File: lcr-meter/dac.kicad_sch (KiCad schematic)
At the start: 0 parts

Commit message: Added CM4, basics of functionality started
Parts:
- added Q2: NPN, symbol Simulation_SPICE:NPN
- added Q3: PNP, symbol Simulation_SPICE:PNP
- added U1: MCP4921, symbol Analog_DAC:MCP4921
- added U3: MCP601-xOT, Package_TO_SOT_SMD:SOT-23-5, symbol Amplifier_Operational:MCP601-xOT
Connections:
- new net: Q2.2 (B), Q3.2 (B), U3.1
- new net: U1.8 (Vout), U3.3 (+)
- new net +5V: Q2.1 (C), U1.1 (Vdd), U1.6 (Vref), U3.5 (V+)
- new net DAC_SCK: U1.3 (SCK)
- new net DAC_SDI: U1.4 (SDI)
- new net DAC_nCS: U1.2 (~{CS})
- new net GND: Q3.1 (C), U1.5 (~{LDAC}), U1.7 (Vss), U3.2 (V-)
- new net Vout: Q2.3 (E), Q3.3 (E), U3.4 (-)

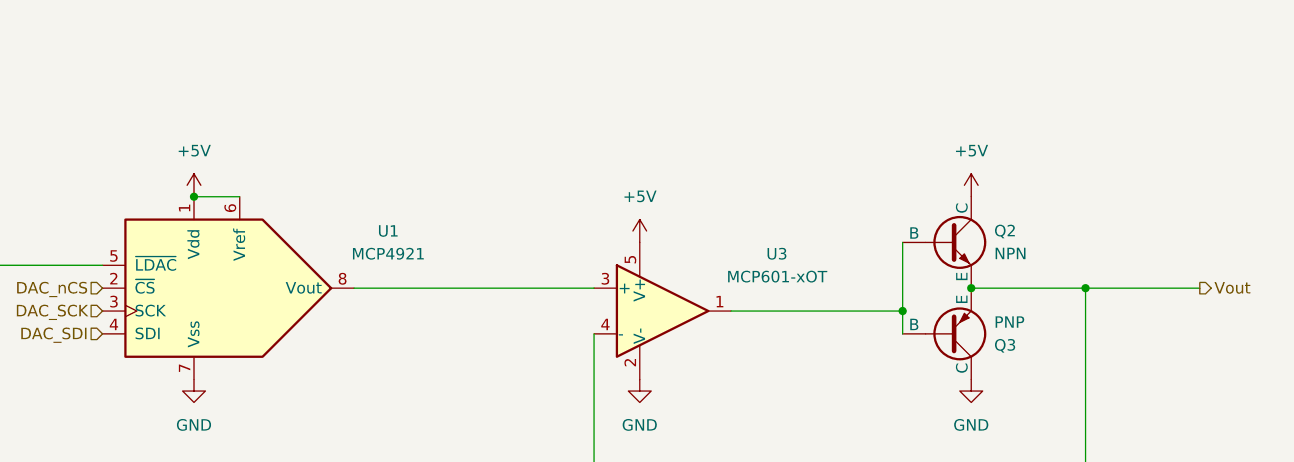
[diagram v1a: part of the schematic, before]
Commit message: Progress, removal of unnecessary components
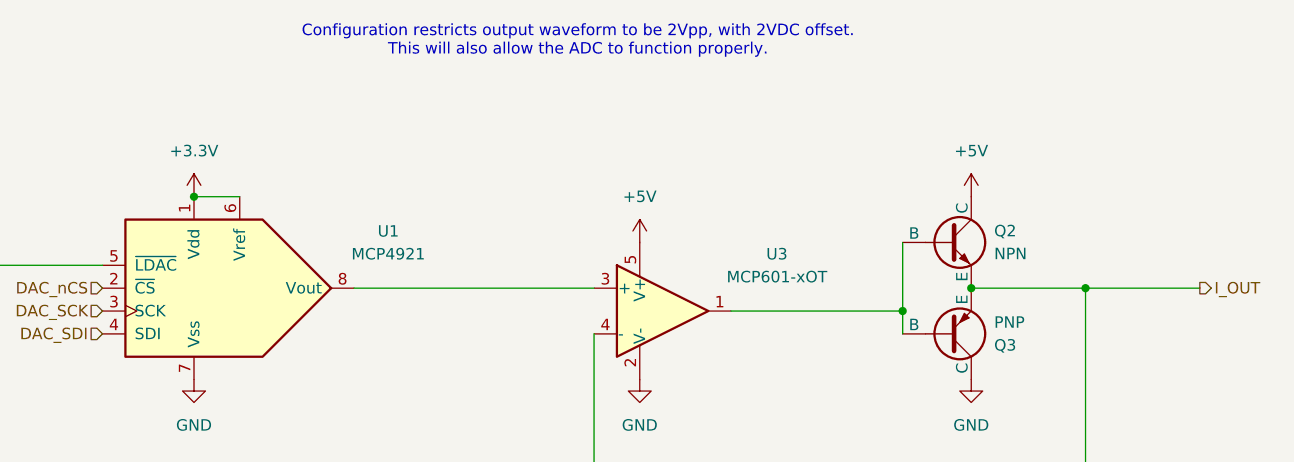
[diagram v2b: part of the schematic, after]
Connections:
- net +5V: no longer U1.1 (Vdd), U1.6 (Vref)
- net Vout renamed I_OUT
- new net +3.3V: U1.1 (Vdd), U1.6 (Vref)
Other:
- note added: "Configuration restricts output waveform to be 2Vpp, with 2VDC offset. This will also allow the ADC to function properly."

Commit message: Breadboarding notes
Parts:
- added U19: AD9833xRM, Package_SO:MSOP-10_3x3mm_P0.5mm, symbol Interface:AD9833xRM
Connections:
- net GND: no longer Q3.1 (C)
- new net -5V: Q3.1 (C)
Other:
- note added: "In testing - BC337"
- note added: "In testing - PN2907A"
- note added: "REPLACE WITH DEDICATED SIGNAL GEN IC AD9833"
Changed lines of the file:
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@@
+		)
+	)
+	(text "In testing - PN2907A"
+		(exclude_from_sim no)
+		(at 232.156 97.79 0)
+		(effects
+			(font
+				(size 1.27 1.27)
+			)
+		)
+	)
+	(text "In testing - BC337"
+		(exclude_from_sim no)
+		(at 232.918 79.248 0)
+		(effects
+			(font
+				(size 1.27 1.27)
+			)
+		)
+	)
+	(text "REPLACE WITH DEDICATED SIGNAL GEN IC\nAD9833"
+		(exclude_from_sim no)
+		(at 101.346 109.982 0)
+		(effects
+			(font
+				(size 1.27 1.27)
+			)
+			(justify left)
 		)
 	)
@@
 	)
 	(symbol
+		(lib_id "power:-5V")
+		(at 213.36 99.06 180)
+		(unit 1)
+		(exclude_from_sim no)
+		(in_bom yes)
+		(on_board yes)
+		(dnp no)
+		(fields_autoplaced yes)
+		(property "Reference" "#PWR059"
+			(at 213.36 95.25 0)
+			(effects
+				(font
+					(size 1.27 1.27)
+				)
+				(hide yes)
+			)
+		)
+		(property "Value" "-5V"
+			(at 213.36 104.14 0)
+			(effects
+				(font
+					(size 1.27 1.27)
+				)
+			)
+		)
+		(property "Footprint" ""
+			(at 213.36 99.06 0)
+			(effects
+				(font
+					(size 1.27 1.27)
+				)
+				(hide yes)
+			)
+		)
+		(property "Datasheet" ""
+			(at 213.36 99.06 0)
+			(effects
+				(font
+					(size 1.27 1.27)
+				)
+				(hide yes)
+			)
+		)
+		(property "Description" "Power symbol creates a global label with name \"-5V\""
+			(at 213.36 99.06 0)
+			(effects
+				(font
+					(size 1.27 1.27)
+				)
+				(hide yes)
+			)
+		)
+		(pin "1"
+		)
+		(instances
+			(project ""
+				(path "/ba333b18-b098-477b-9dd4-aab7b9764d9c/46ee5347-8922-4c9f-a4b3-4d37bef42e8e"
+					(reference "#PWR059")
+					(unit 1)
+				)
+			)
+		)
+	)
+	(symbol
 		(lib_id "power:GND")
 		(at 127 99.06 0)
@@
 	)
 	(symbol
-		(lib_id "power:GND")
-		(at 213.36 99.06 0)
-		(unit 1)
-		(exclude_from_sim no)
-		(in_bom yes)
-		(on_board yes)
-		(dnp no)
-		(fields_autoplaced yes)
-		(property "Reference" "#PWR036"
-			(at 213.36 105.41 0)
-			(effects
-				(font
-					(size 1.27 1.27)
-				)
-				(hide yes)
-			)
-		)
-		(property "Value" "GND"
-			(at 213.36 104.14 0)
-			(effects
-				(font
-					(size 1.27 1.27)
-				)
-			)
-		)
-		(property "Footprint" ""
-			(at 213.36 99.06 0)
-			(effects
-				(font
-					(size 1.27 1.27)
-				)
-				(hide yes)
-			)
-		)
-		(property "Datasheet" ""
-			(at 213.36 99.06 0)
-			(effects
-				(font
-					(size 1.27 1.27)
-				)
-				(hide yes)
-			)
-		)
-		(property "Description" "Power symbol creates a global label with name \"GND\" , ground"
-			(at 213.36 99.06 0)
-			(effects
-				(font
-					(size 1.27 1.27)
-				)
-				(hide yes)
-			)
-		)
-		(pin "1"
-		)
-		(instances
-			(project "lcr-meter"
-				(path "/ba333b18-b098-477b-9dd4-aab7b9764d9c/46ee5347-8922-4c9f-a4b3-4d37bef42e8e"
-					(reference "#PWR036")
-					(unit 1)
-				)
+		(lib_id "Interface:AD9833xRM")
+		(at 127 130.81 0)
+		(unit 1)
+		(exclude_from_sim no)
+		(in_bom yes)
+		(on_board yes)
+		(dnp no)
+		(fields_autoplaced yes)
+		(property "Reference" "U19"
+			(at 146.05 121.9514 0)
+			(effects
+				(font
+					(size 1.27 1.27)
+				)
+			)
+		)
+		(property "Value" "AD9833xRM"
+			(at 146.05 124.4914 0)
+			(effects
+				(font
+					(size 1.27 1.27)
+				)
+			)
+		)
+		(property "Footprint" "Package_SO:MSOP-10_3x3mm_P0.5mm"
+			(at 127 146.05 0)
+			(effects
+				(font
+					(size 1.27 1.27)
+				)
+				(hide yes)
+			)
+		)
+		(property "Datasheet" "https://www.analog.com/media/en/technical-documentation/data-sheets/ad9833.pdf"
+			(at 125.73 123.19 0)
+			(effects
+				(font
+					(size 1.27 1.27)
+				)
+				(hide yes)
+			)
+		)
+		(property "Description" "10 bit 25 MHz Programmable Waveform Generator, 2.3V to 5.5V, 12.65mW, MSOP-10"
+			(at 127 130.81 0)
+			(effects
+				(font
+					(size 1.27 1.27)
+				)
+				(hide yes)
+			)
+		)
+		(pin "6"
+		)
+		(pin "4"
+		)
+		(pin "7"
+		)
+		(pin "9"
+		)
+		(pin "5"
+		)
+		(pin "1"
+		)
+		(pin "2"
+		)
+		(pin "10"
+		)
+		(pin "3"
+		)
+		(pin "8"
+		)
+		(instances
+			(project ""
+				(path "/ba333b18-b098-477b-9dd4-aab7b9764d9c/46ee5347-8922-4c9f-a4b3-4d37bef42e8e"
+					(reference "U19")
+					(unit 1)
+				)

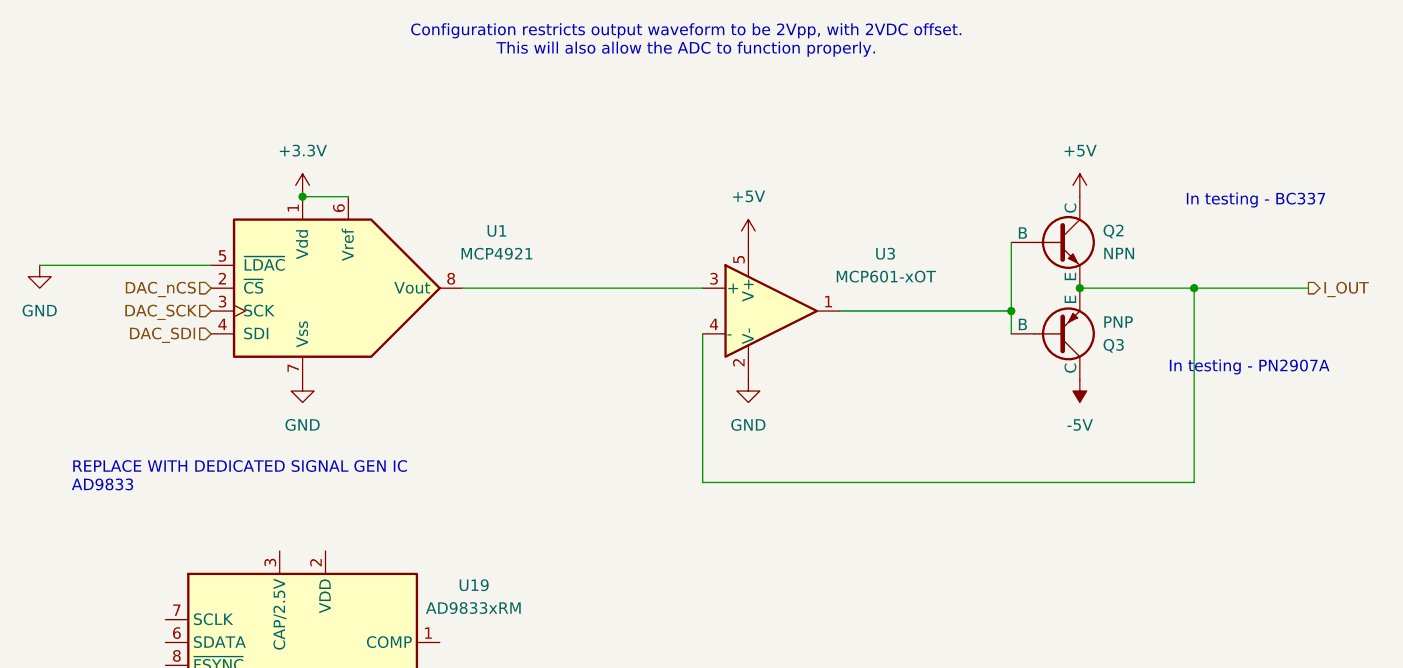
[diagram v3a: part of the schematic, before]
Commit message: Schematic updates, added -5V, finalized sensing
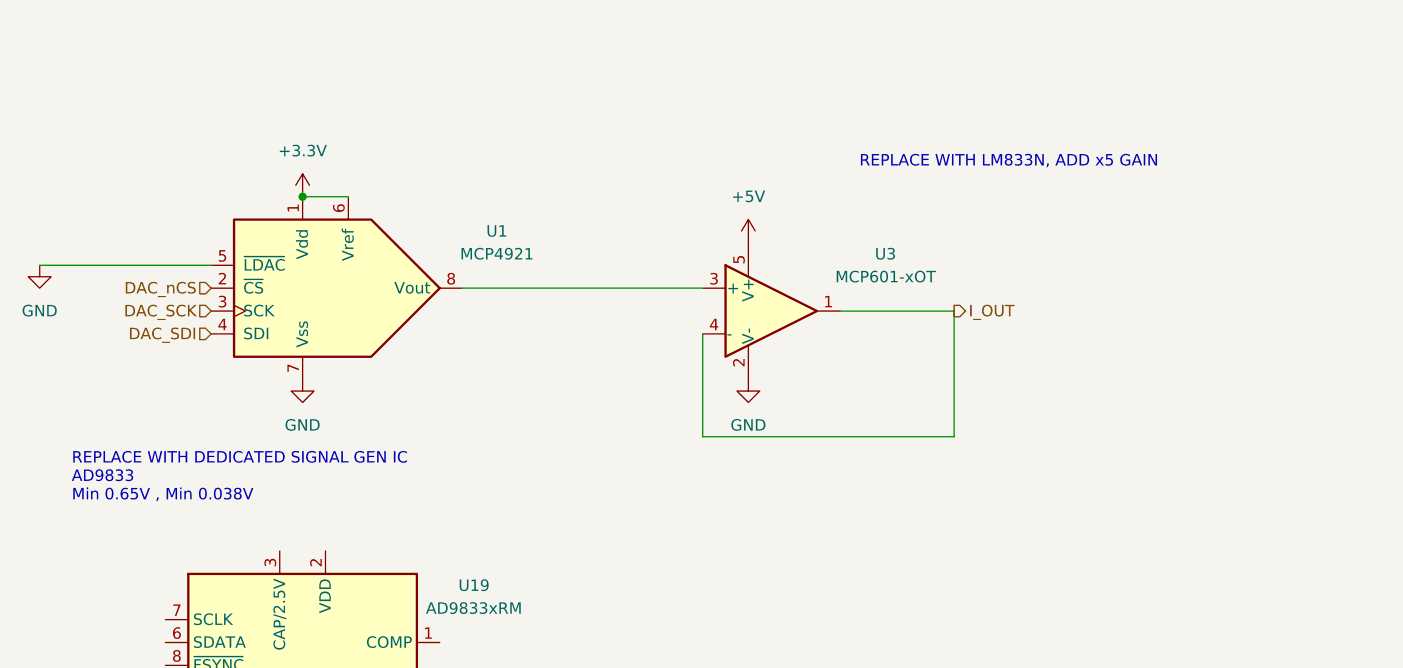
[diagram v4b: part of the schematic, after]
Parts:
- removed Q2: NPN, symbol Simulation_SPICE:NPN
- removed Q3: PNP, symbol Simulation_SPICE:PNP
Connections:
- net I_OUT: now also U3.1
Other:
- note added: "REPLACE WITH DEDICATED SIGNAL GEN IC AD9833 Min 0.65V , Min 0.038V"
- note added: "REPLACE WITH LM833N, ADD x5 GAIN"
- note removed: "Configuration restricts output waveform to be 2Vpp, with 2VDC offset. This will also allow the ADC to function properly."
- note removed: "In testing - BC337"
- note removed: "In testing - PN2907A"
- note removed: "REPLACE WITH DEDICATED SIGNAL GEN IC AD9833"

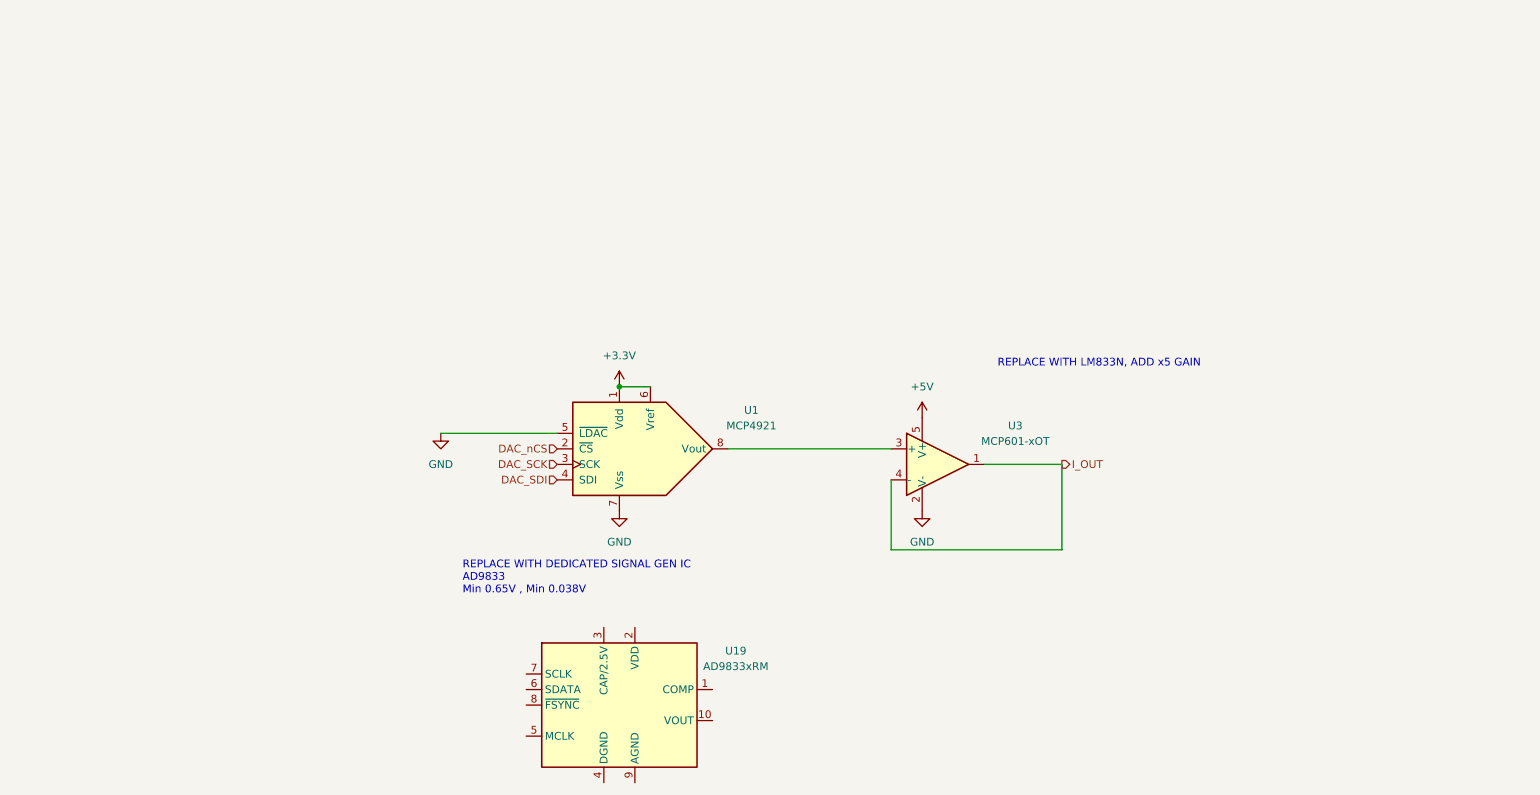
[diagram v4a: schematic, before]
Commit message: Addressable LED test board
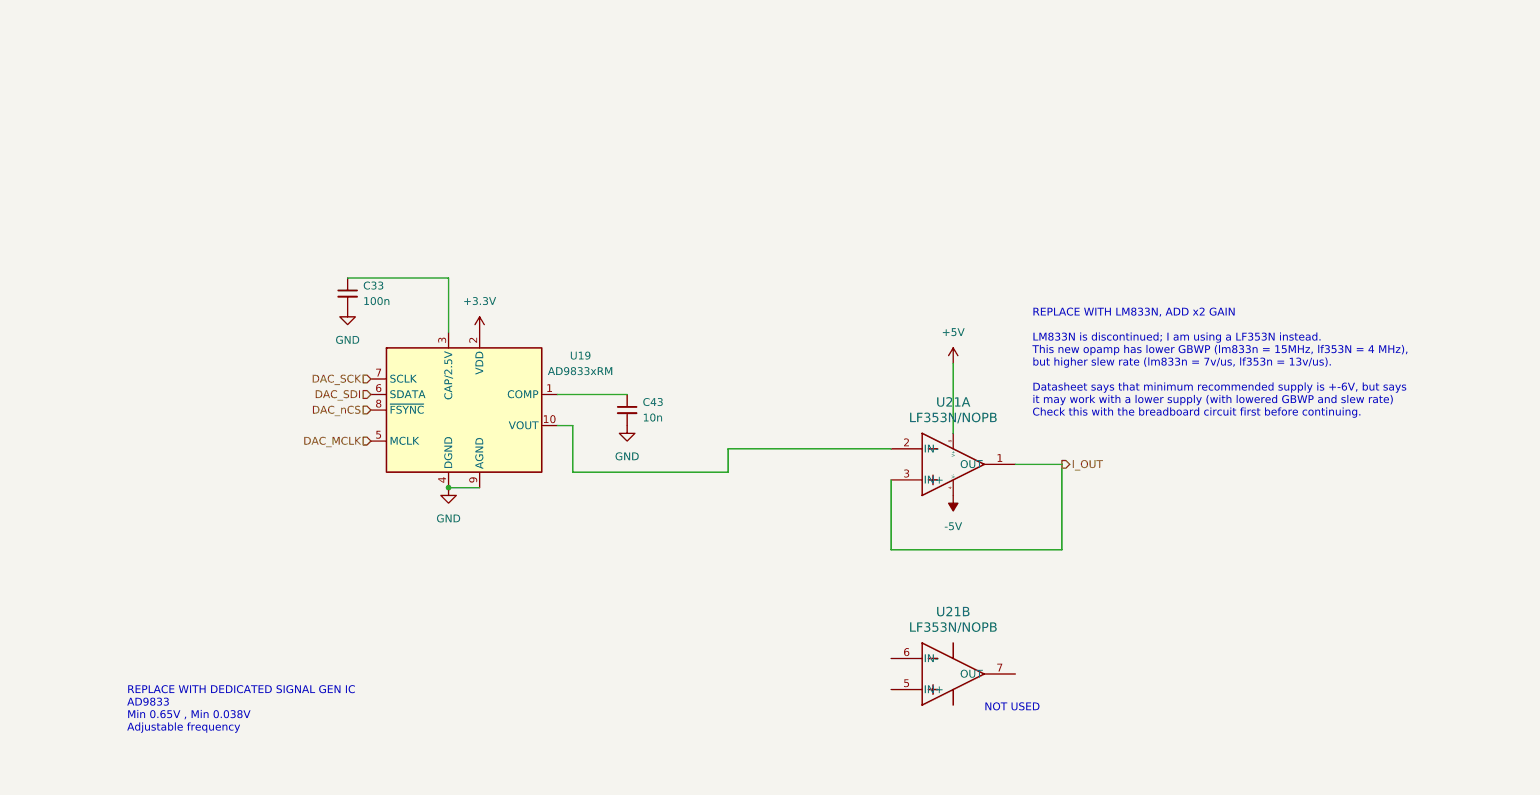
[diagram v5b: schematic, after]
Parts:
- removed U1: MCP4921, symbol Analog_DAC:MCP4921
- removed U3: MCP601-xOT, Package_TO_SOT_SMD:SOT-23-5, symbol Amplifier_Operational:MCP601-xOT
- added C33: 100n, symbol Device:C_Small
- added C43: 10n, symbol Device:C_Small
- added U21: LF353N/NOPB, N08E, symbol 2024-10-13_18-48-05:LF353N_NOPB
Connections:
- net +3.3V: now also U19.2 (VDD)
- net +5V: now also U21.8 (V+)
- net DAC_SCK: now also U19.7 (SCLK)
- net DAC_SDI: now also U19.6 (SDATA)
- net DAC_nCS: now also U19.8 (~{FSYNC})
- net GND: now also U19.4 (DGND), U19.9 (AGND), C33.2, C43.2
- net I_OUT: now also U21.1 (OUT), U21.3 (IN+)
- net at U19.1 (COMP): now also C43.1
- net at U19.10 (VOUT): now also U21.2 (IN-)
- net at U19.3 (CAP/2.5V): now also C33.1
- net DAC_MCLK: now reaches U19.5 (MCLK)
- new net -5V: U21.4 (V-)
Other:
- note added: "NOT USED"
- note added: "REPLACE WITH DEDICATED SIGNAL GEN IC AD9833 Min 0.65V , Min 0.038V Adjustable frequency"
- note added: "REPLACE WITH LM833N, ADD x2 GAIN LM833N is discontinued; I am using a LF353N instead. This new opamp has lower GBWP (lm833n = 15MHz, lf353N = 4 MHz), but higher slew rate (lm833n = 7v/us, lf353n = 13v/us). Datasheet says that minimum recommended supply is +-6V, but says it may work with a lower supply (with lowered GBWP and slew rate) Check this with the breadboard circuit first before continuing."
- note removed: "REPLACE WITH DEDICATED SIGNAL GEN IC AD9833 Min 0.65V , Min 0.038V"
- note removed: "REPLACE WITH LM833N, ADD x5 GAIN"
- moved on the sheet: U19

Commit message: Schematic polishing, starting MCU schematic
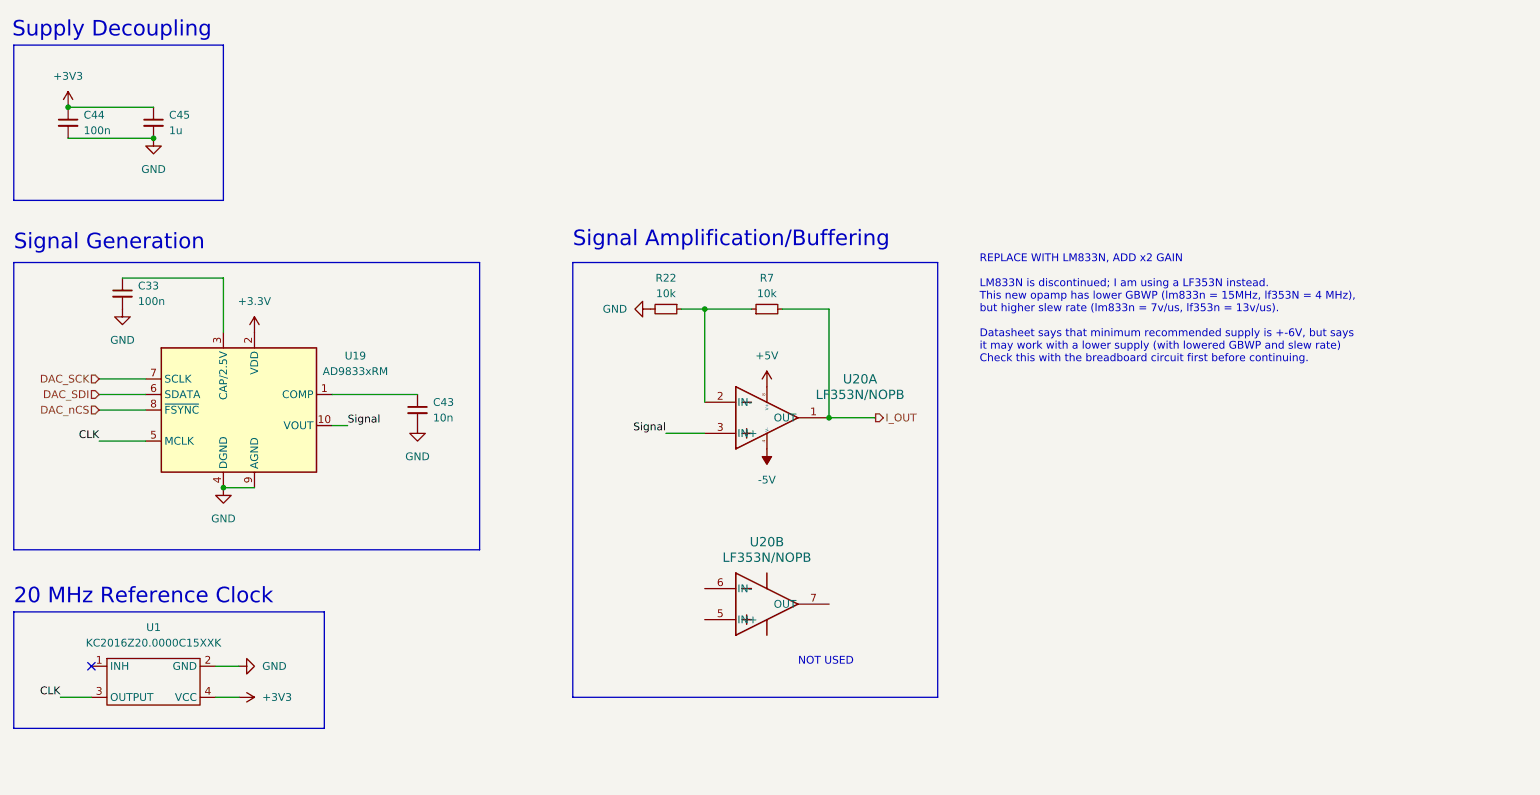
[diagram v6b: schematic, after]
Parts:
- removed U21: LF353N/NOPB, N08E, symbol 2024-10-13_18-48-05:LF353N_NOPB
- added C44: 100n, Capacitor_SMD:C_0402_1005Metric, symbol Device:C_Small
- added C45: 1u, Capacitor_SMD:C_0402_1005Metric, symbol Device:C_Small
- added R22, R7: 10k, symbol Device:R_Small
- added U1: KC2016Z20.0000C15XXK, Crystal:Crystal_SMD_2016-4Pin_2.0x1.6mm, symbol KC2016Z:KC2016Z20.0000C15XXK
- added U20: LF353N/NOPB, N08E, symbol 2024-10-13_18-48-05:LF353N_NOPB
- C33, C43: footprint (none) -> Capacitor_SMD:C_0402_1005Metric
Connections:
- net +5V: now also U20.8 (V+)
- net -5V: now also U20.4 (V-)
- net GND: now also C44.2, C45.2, R22.2, U1.2 (GND)
- net I_OUT: now also R7.2, U20.1 (OUT)
- net Signal: now reaches U19.10 (VOUT)
- net Signal: now also U20.3 (IN+)
- net DAC_MCLK renamed CLK
- net CLK: now also U1.3 (OUTPUT)
- new net: R22.1, R7.1, U20.2 (IN-)
- new net +3V3: C44.1, C45.1, U1.4 (VCC)
- no-connect marks 0 -> 1
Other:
- note added: "20 MHz Reference Clock"
- note added: "Signal Amplification/Buffering"
- note added: "Signal Generation"
- note added: "Supply Decoupling"
- note removed: "REPLACE WITH DEDICATED SIGNAL GEN IC AD9833 Min 0.65V , Min 0.038V Adjustable frequency"
- moved on the sheet: C33, C43, U19
